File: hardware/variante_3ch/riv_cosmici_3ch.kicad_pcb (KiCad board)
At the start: 2 copper layers, 95 x 205 mm, 178 parts, among them J101 SiPM_CH1, J104 LEMO_CH1, J201 SiPM_CH2, J204 LEMO_CH2, J3 PWR_5V, J301 SiPM_CH3, J304 LEMO_CH3, J5 LEMO_AND, Q101 BFR93A, Q102 MMBTH81, Q201 BFR93A, Q202 MMBTH81, Q301 BFR93A, Q302 MMBTH81, U1 LT3461, U10 74LVC1G11, U102 TLC555/LMC555, U103 MAX961, U108 LT1636, U109 74LVC1G17, U202 TLC555/LMC555, U203 MAX961, U208 LT1636, U209 74LVC1G17, U302 TLC555/LMC555, U303 MAX961, U308 LT1636, U309 74LVC1G17, U5 LP2985AIM5-3.6, U6 MCP1825S-3302, U7 LP2985AIM5-3.6

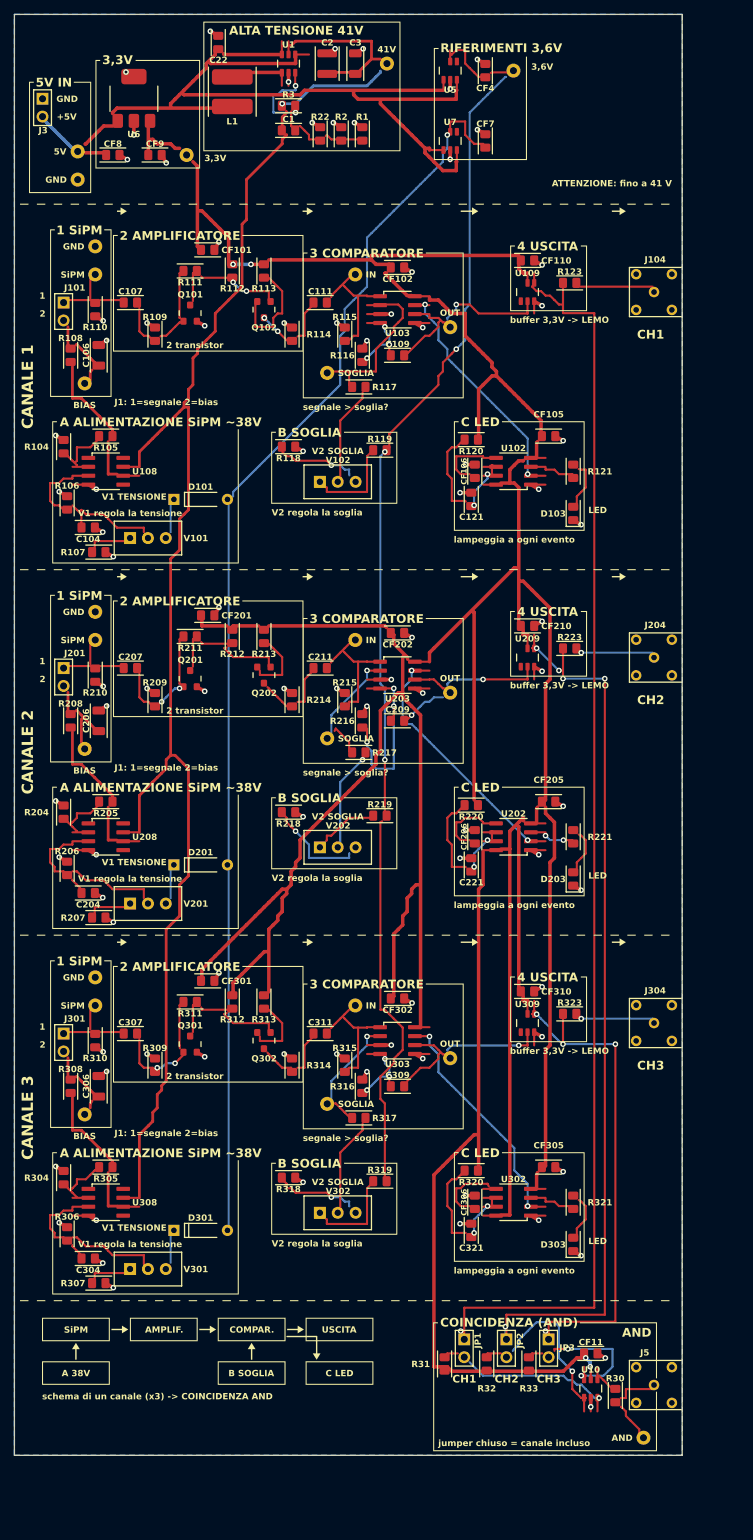
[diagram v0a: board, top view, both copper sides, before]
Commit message: Variante 3ch: monitor delle tensioni dei SiPM (ADC MCP3424 in I2C)
- partitori 1M/43k + 100n su VREG38 di ogni canale e sull'alta tensione
- ADC MCP3424 (U11, 0x68), resistenze serie 100R su SDA/SCL, connettore J6
- router: le linee MON stanno a >= 1,2 mm dai nodi analogici sensibili su
  entrambi gli strati (misurato: 1,6 mm); piste dei segnali invariate
- simulazione: con il monitor bias, impulsi e soglia restano identici
- software/monitor_tensioni.py per il Raspberry Pi
- footprint SOIC14 e HDR1x03, simboli MCP3424 e CONN3; stub dei SOIC dal lato lungo

Co-Authored-By: Claude Opus 5.5 <noreply@anthropic.com>
Claude-Session: https://claude.ai/code/session_017fc9yPsNewCQrMK8R1c8Ls
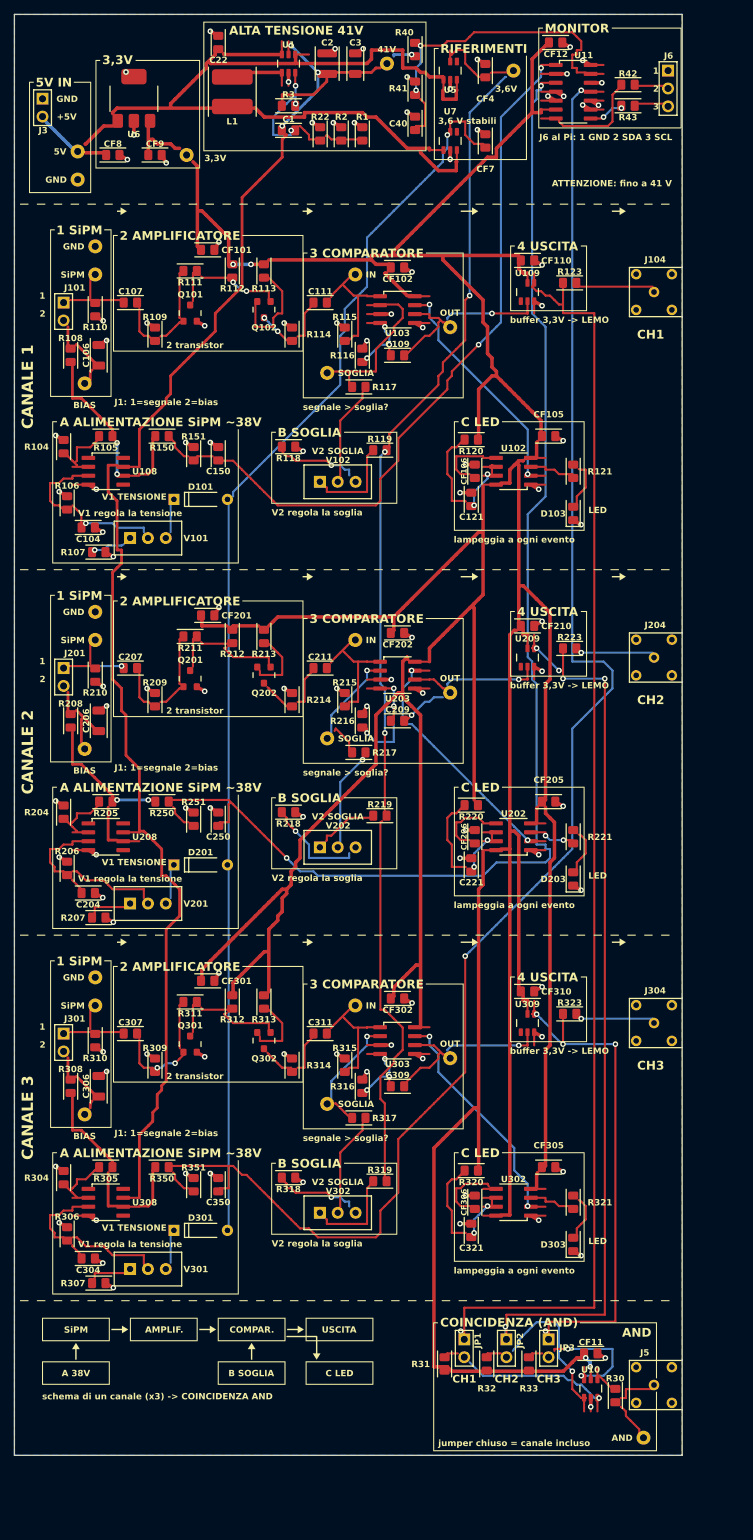
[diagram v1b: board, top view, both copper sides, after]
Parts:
- added C150: 100n, rivlib:C_0805, F.Cu at (49.0, 82.5)
- added C250: 100n, rivlib:C_0805, F.Cu at (49.0, 134.5)
- added C350: 100n, rivlib:C_0805, F.Cu at (49.0, 186.5)
- added C40: 100n, rivlib:C_0805, F.Cu at (77.0, 35.5)
- added CF12: 100n, rivlib:C_0805, F.Cu at (97.0, 24.0)
- added J6: I2C_RPI, rivlib:HDR1x03, F.Cu at (113.0, 28.0)
- added R150: 1M, rivlib:R_0805, F.Cu at (41.0, 80.0)
- added R151: 43k, rivlib:R_0805, F.Cu at (45.5, 82.5)
- added R250: 1M, rivlib:R_0805, F.Cu at (41.0, 132.0)
- added R251: 43k, rivlib:R_0805, F.Cu at (45.5, 134.5)
- added R350: 1M, rivlib:R_0805, F.Cu at (41.0, 184.0)
- added R351: 43k, rivlib:R_0805, F.Cu at (45.5, 186.5)
- added R40: 1M, rivlib:R_0805, F.Cu at (77.0, 25.0)
- added R41: 43k, rivlib:R_0805, F.Cu at (77.0, 30.5)
- added R42: 100R, rivlib:R_0805, F.Cu at (107.3, 30.0)
- added R43: 100R, rivlib:R_0805, F.Cu at (107.3, 33.0)
- added U11: MCP3424, rivlib:SOIC14, F.Cu at (99.5, 31.0)
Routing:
- net MON3: track 0.00 -> 227.0 mm, vias 0 -> 2
- net MON2: track 0.00 -> 185.4 mm, vias 0 -> 2
- net MON1: track 0.00 -> 106.8 mm, vias 0 -> 2
- net +3V3: track 682.4 -> 775.5 mm
- net MON4: track 0.00 -> 46.6 mm, vias 0 -> 2
- net GND: track 155.5 -> 190.6 mm, vias 89 -> 105
- net VOUT40: track 236.4 -> 211.6 mm, vias 1 -> 4
- net SDA_ADC: track 0.00 -> 16.1 mm
- net LE2: track 25.0 -> 17.3 mm
- net VREG383: track 21.4 -> 28.6 mm
- net VREG381: track 21.2 -> 27.2 mm, vias 0 -> 2
- net VREG382: track 21.3 -> 26.9 mm, vias 0 -> 2
- net SCL_ADC: track 0.00 -> 5.30 mm, vias 0 -> 2
- net +5V: track 143.6 -> 138.9 mm
- net SIG_IN2: track 9.17 -> 13.5 mm, vias 0 -> 1
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
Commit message: Variante 3ch: disposizione piu' ordinata e fori di fissaggio M3
- scheda 103 x 215 mm: colonne distanziate (>= 2 mm tra i riquadri), spostamenti
  multipli della griglia del router
- serigrafia: riquadri della stessa riga con bordi allineati, titoli fissi,
  sottotitoli sotto il riquadro, frecce del segnale calcolate tra i blocchi,
  avviso 41 V nel blocco ALTA TENSIONE
- 8 fori M3 metallizzati a massa (angoli e confini tra i canali)
- routing rifatto: 0 errori DRC/connettivita', monitor a 1,6 mm dai nodi sensibili
- render, PDF, presentazione aggiornati

Co-Authored-By: Claude Opus 5.5 <noreply@anthropic.com>
Claude-Session: https://claude.ai/code/session_017fc9yPsNewCQrMK8R1c8Ls
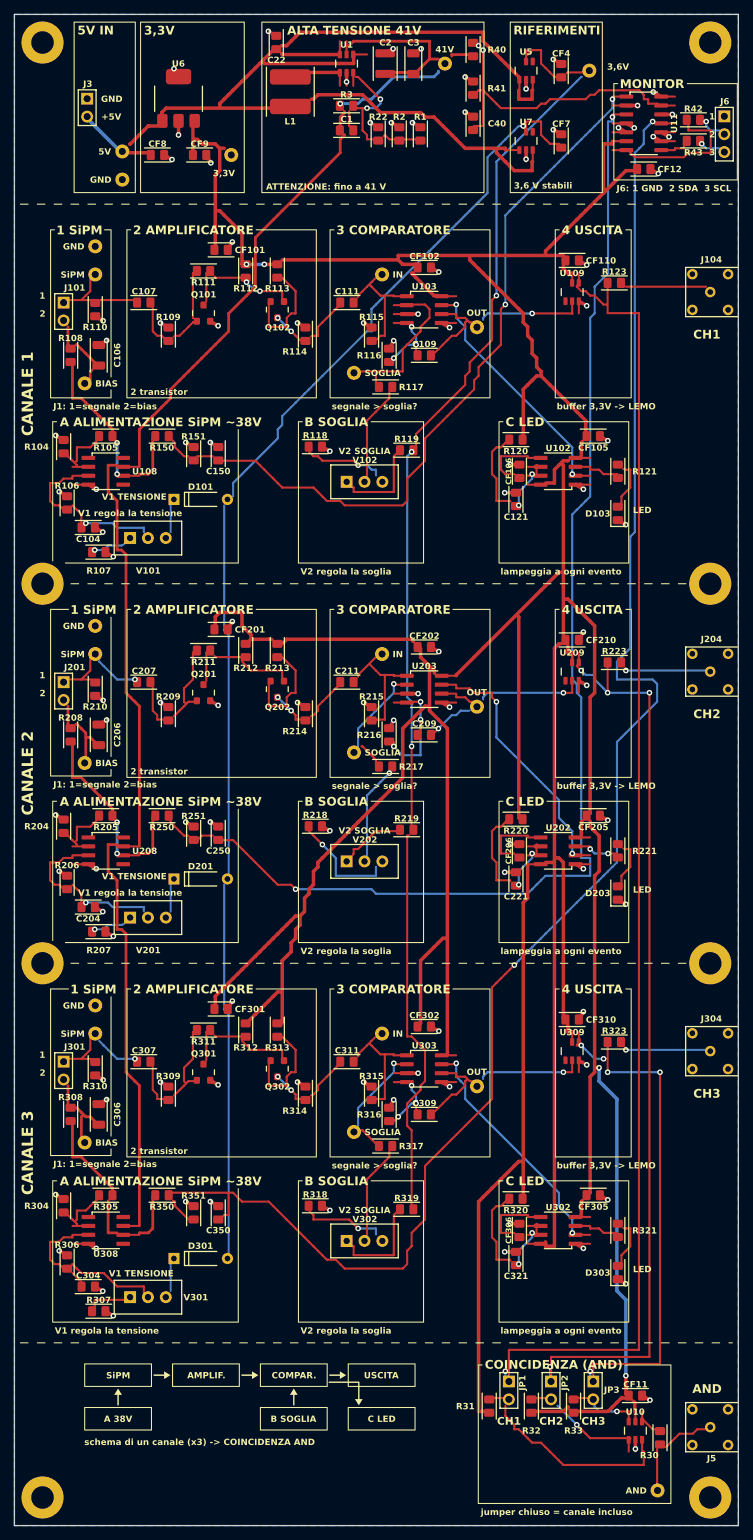
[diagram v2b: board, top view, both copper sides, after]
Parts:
- added MH1: M3, rivlib:MH_M3, F.Cu at (24.0, 24.0)
- added MH2: M3, rivlib:MH_M3, F.Cu at (119.0, 24.0)
- added MH3: M3, rivlib:MH_M3, F.Cu at (24.0, 231.0)
- added MH4: M3, rivlib:MH_M3, F.Cu at (119.0, 231.0)
- added MH5: M3, rivlib:MH_M3, F.Cu at (24.0, 101.0)
- added MH6: M3, rivlib:MH_M3, F.Cu at (119.0, 101.0)
- added MH7: M3, rivlib:MH_M3, F.Cu at (24.0, 155.0)
- added MH8: M3, rivlib:MH_M3, F.Cu at (119.0, 155.0)
- moved CF12 21.9 mm to (109.5, 42.0)
- moved U11 11.0 mm to (109.5, 35.5)
- moved CF4 10.8 mm to (97.8, 28.0)
- moved CF7 10.8 mm to (97.8, 38.0)
- moved TP4 10.8 mm to (101.8, 28.0)
- moved U5 10.8 mm to (92.8, 28.0)
- moved U7 10.8 mm to (92.8, 38.0)
- moved R42 10.6 mm to (116.6, 35.0)
- moved R43 10.6 mm to (116.6, 38.0)
- moved J6 10.3 mm to (121.0, 34.5)
- moved J5 10.0 mm to (119.0, 221.0)
- moved J304 8.94 mm to (119.0, 167.5)
- moved CF11 8.74 mm to (108.3, 216.5)
- moved JP1 8.74 mm to (90.3, 214.5)
- moved JP2 8.74 mm to (96.3, 214.5)
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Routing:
- net +3V3: track 775.5 -> 812.7 mm
- net +5V: track 138.9 -> 156.6 mm
- net VOUT40: track 211.6 -> 227.7 mm, vias 4 -> 1
- net AND_IN3: track 21.2 -> 8.68 mm, vias 2 -> 1
- net VREF_B: track 175.5 -> 186.7 mm
- net AND_IN2: track 25.7 -> 15.6 mm
- net MON3: track 227.0 -> 234.3 mm
- net +3V6: track 180.0 -> 186.4 mm
- net MON2: track 185.4 -> 179.2 mm
- net SDA_ADC: track 16.1 -> 21.9 mm
- net Q2E2: track 9.04 -> 14.4 mm
- net Q2E3: track 9.06 -> 14.4 mm
- net BUF_Y1: track 182.2 -> 187.5 mm
- net AND_IN1: track 24.9 -> 30.2 mm, vias 1 -> 0
- net SIG_IN3: track 9.06 -> 13.2 mm, vias 0 -> 1
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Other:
- board size 95 x 205 mm -> 103 x 215 mm

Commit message: 3 canali: connettore barra Molex KK 254 (J101/J201/J301), PCB, Gerber, JLC, PDF, librerie e render aggiornati
Footprint MOLEX_KK_2 con gli stessi fori della strip (routing invariato),
etichette 1/2 della serigrafia spostate fuori dal corpo, modello 3D del
connettore nel viewer, zip KiCad autosufficiente con librerie aggiornate.

Co-Authored-By: Claude Opus 5.5 <noreply@anthropic.com>
Claude-Session: https://claude.ai/code/session_017fc9yPsNewCQrMK8R1c8Ls
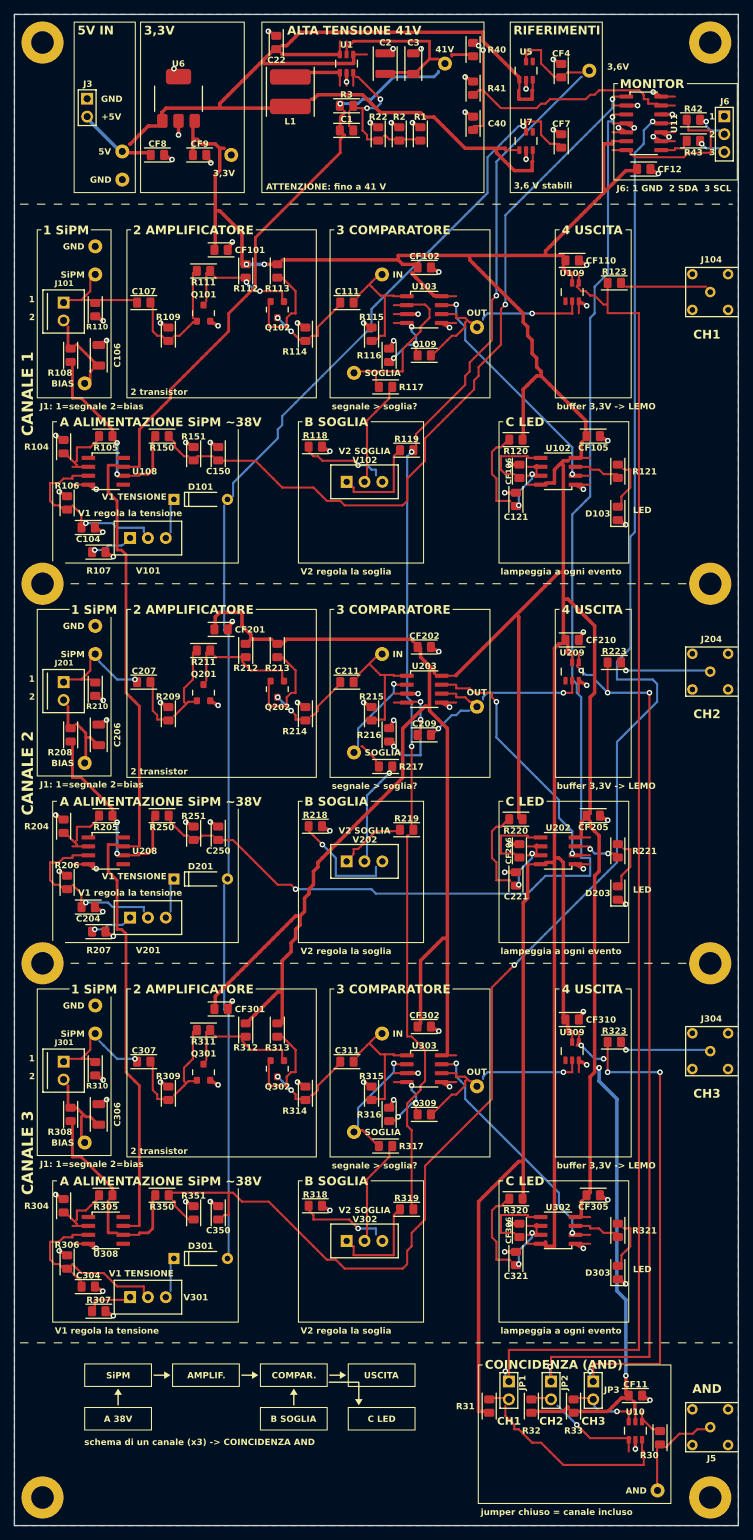
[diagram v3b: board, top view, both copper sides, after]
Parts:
- J101, J201, J301: footprint rivlib:HDR1x02 -> rivlib:MOLEX_KK_2

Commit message: Verifica con KiCad 7: corretti collegamenti ai pad, isole di massa e giunzioni dello schema
Il DRC di KiCad ha trovato reti aperte che il controllo interno non vedeva:
- piste che toccavano solo l'angolo del rettangolo d'ingombro di pad tondi o
  arrotondati: ora ogni pista viene prolungata fino al centro del pad
  (gen_pcb.snap_to_pads) e la connettivita' si controlla sulla forma reale;
  pad SMD rettangolari anche in KiCad, come nei Gerber;
- isole del piano di massa staccate (prima i pezzi del piano contavano come uno):
  niente colli sotto 0,3 mm, reti che chiudono le isole ri-instradate per prime,
  pista di massa aggiunta sulla scheda a 3 canali; scheda a 1 canale ri-instradata;
- giunzioni a T nello schema (Q1C, LE) non collegate da KiCad: fili spezzati in
  ogni giunzione.

Nuovo generator/verifica_kicad.py: netlist dello schema (kicad-cli) = PCB, DRC di
KiCad, connettivita' sul rame reale. Entrambe le schede: OK.
Gerber, JLCPCB, zip KiCad, PDF e render rigenerati.

Co-Authored-By: Claude Opus 5.5 <noreply@anthropic.com>
Claude-Session: https://claude.ai/code/session_017fc9yPsNewCQrMK8R1c8Ls
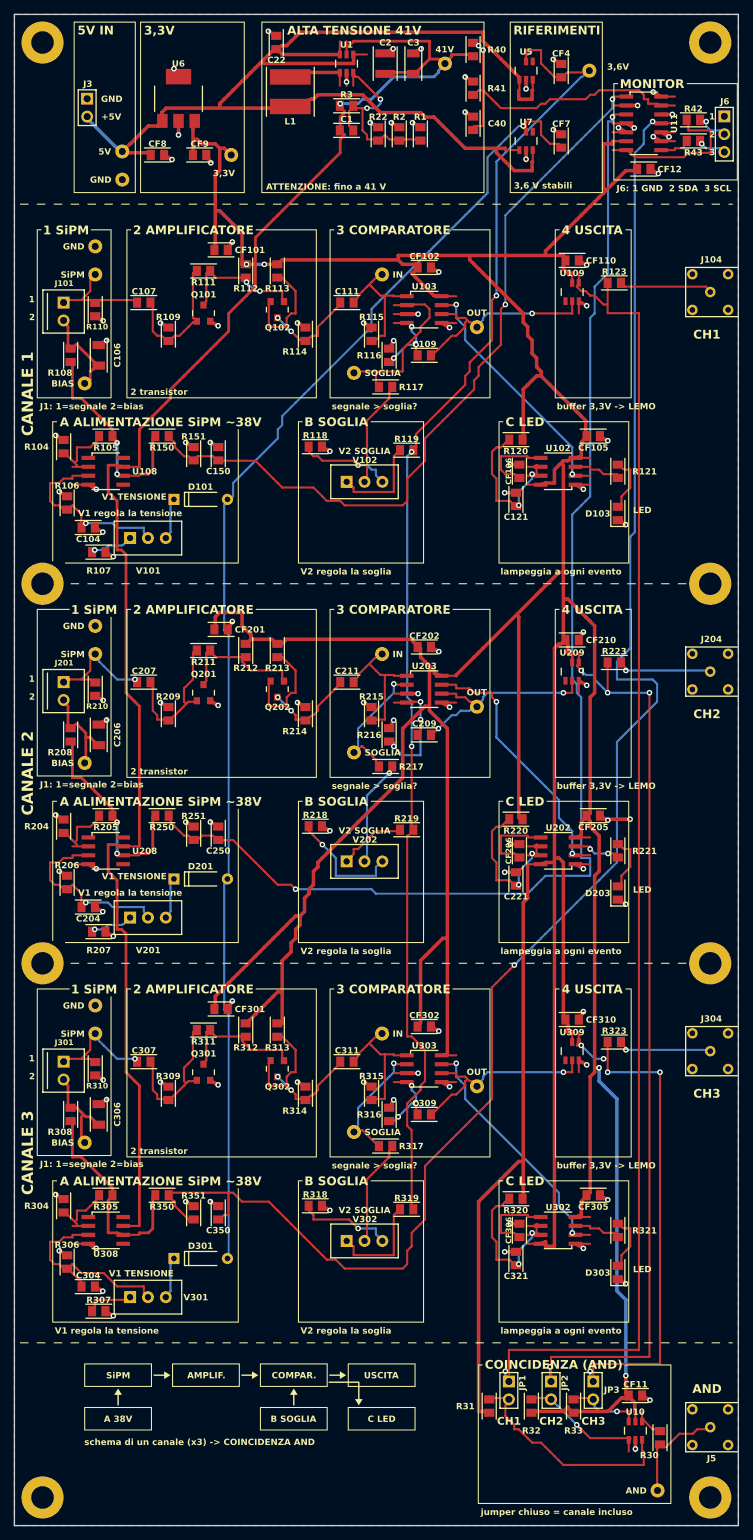
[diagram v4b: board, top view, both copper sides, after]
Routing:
- net +3V3: track 812.7 -> 840.6 mm
- net +5V: track 156.6 -> 170.4 mm
- net GND: track 190.1 -> 201.1 mm, vias 105 -> 106
- net VOUT40: track 227.7 -> 236.9 mm
- net SIG_IN3: track 13.2 -> 17.6 mm
- net SIG_IN2: track 13.2 -> 17.6 mm
- net BIAS1: track 9.25 -> 13.3 mm
- net VREF_B: track 186.7 -> 190.2 mm
- net SIG_IN1: track 11.9 -> 15.4 mm
- net FB: track 25.9 -> 29.4 mm
- net +3V6: track 186.4 -> 189.8 mm
- net CMP_Q2: track 27.2 -> 30.5 mm
- net SW: track 6.08 -> 9.10 mm
- net Q1C1: track 16.4 -> 19.4 mm
- net AND_IN2: track 15.6 -> 18.4 mm
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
